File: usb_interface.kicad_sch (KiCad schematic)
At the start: 13 parts, among them J2 USB_B_Micro, U4 FT234XD-R

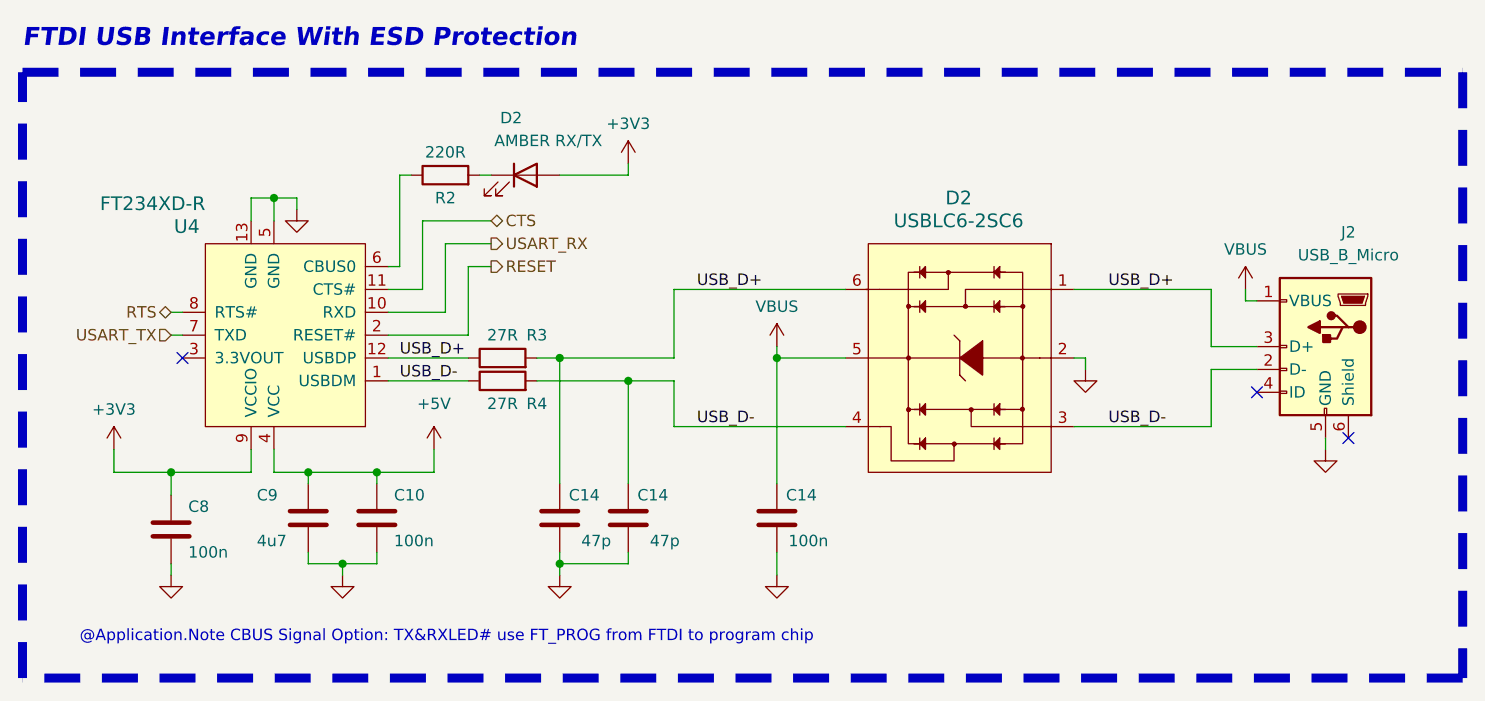
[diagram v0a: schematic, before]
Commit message: Added all schmatics about to change LDO 1 to buck
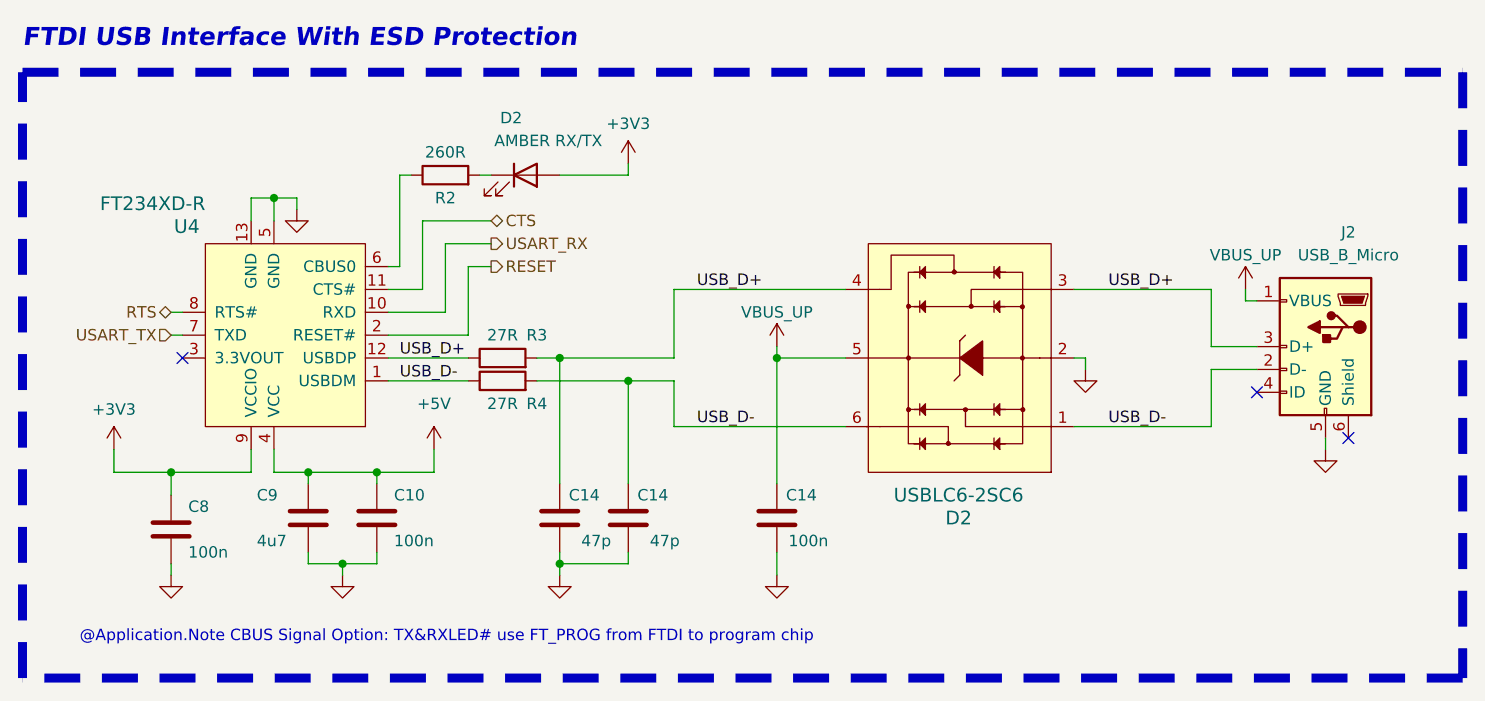
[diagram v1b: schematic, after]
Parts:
- C9: footprint Capacitor_SMD:C_0402_1005Metric -> Capacitor_SMD:C_0603_1608Metric
- J2: footprint Connector_USB:USB_Micro-B_Amphenol_10103594-0001LF_Horizontal -> Connector_USB:USB_Micro-B_Amphenol_10118194_Horizontal
- R2: value 220R -> 260R; footprint Resistor_SMD:R_0402_1005Metric -> Resistor_SMD:R_0603_1608Metric
- R3, R4: footprint Resistor_SMD:R_0402_1005Metric -> Resistor_SMD:R_0603_1608Metric
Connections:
- net USB_D+: now also D2.3, D2.4; no longer D2.1, D2.6
- net USB_D-: now also D2.1, D2.6; no longer D2.3, D2.4
- net VBUS renamed VBUS_UP
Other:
- moved on the sheet: D2
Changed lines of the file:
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@@
     (effects (font (size 1.27 1.27)) (justify left))
   )
-  (symbol (lib_id "dk_TVS-Diodes:USBLC6-2SC6") (at 127 86.36 0) (mirror y) (unit 1)
-    (in_bom yes) (on_board yes) (dnp no)
-    (property "Reference" "D2" (at 126.873 68.58 0)
+  (symbol (lib_id "dk_TVS-Diodes:USBLC6-2SC6") (at 127 86.36 180) (unit 1)
+    (in_bom yes) (on_board yes) (dnp no)
+    (property "Reference" "D2" (at 126.873 104.14 0)
       (effects (font (size 1.524 1.524)))
     )
-    (property "Value" "USBLC6-2SC6" (at 126.873 71.12 0)
+    (property "Value" "USBLC6-2SC6" (at 126.873 101.6 0)
       (effects (font (size 1.524 1.524)))
     )
-    (property "Footprint" "digikey-footprints:SOT23-6L" (at 121.92 81.28 0)
-      (effects (font (size 1.524 1.524)) (justify left) hide)
-    )
-    (property "Datasheet" "http://www.st.com/content/ccc/resource/technical/document/datasheet/06/1d/48/9c/6c/20/4a/b2/CD00050750.pdf/files/CD00050750.pdf/jcr:content/translations/en.CD00050750.pdf" (at 121.92 78.74 0)
-      (effects (font (size 1.524 1.524)) (justify left) hide)
-    )
-    (property "Digi-Key_PN" "497-5235-1-ND" (at 121.92 76.2 0)
-      (effects (font (size 1.524 1.524)) (justify left) hide)
-    )
-    (property "MPN" "USBLC6-2SC6" (at 121.92 73.66 0)
-      (effects (font (size 1.524 1.524)) (justify left) hide)
-    )
-    (property "Category" "Circuit Protection" (at 121.92 71.12 0)
-      (effects (font (size 1.524 1.524)) (justify left) hide)
-    )
-    (property "Family" "TVS - Diodes" (at 121.92 68.58 0)
-      (effects (font (size 1.524 1.524)) (justify left) hide)
-    )
-    (property "DK_Datasheet_Link" "http://www.st.com/content/ccc/resource/technical/document/datasheet/06/1d/48/9c/6c/20/4a/b2/CD00050750.pdf/files/CD00050750.pdf/jcr:content/translations/en.CD00050750.pdf" (at 121.92 66.04 0)
-      (effects (font (size 1.524 1.524)) (justify left) hide)
-    )
-    (property "DK_Detail_Page" "/product-detail/en/stmicroelectronics/USBLC6-2SC6/497-5235-1-ND/1121688" (at 121.92 63.5 0)
-      (effects (font (size 1.524 1.524)) (justify left) hide)
-    )
-    (property "Description" "TVS DIODE 5.25V 17V SOT23-6" (at 121.92 60.96 0)
-      (effects (font (size 1.524 1.524)) (justify left) hide)
-    )
-    (property "Manufacturer" "STMicroelectronics" (at 121.92 58.42 0)
-      (effects (font (size 1.524 1.524)) (justify left) hide)
-    )
-    (property "Status" "Active" (at 121.92 55.88 0)
+    (property "Footprint" "digikey-footprints:SOT23-6L" (at 121.92 91.44 0)
+      (effects (font (size 1.524 1.524)) (justify left) hide)
+    )
+    (property "Datasheet" "http://www.st.com/content/ccc/resource/technical/document/datasheet/06/1d/48/9c/6c/20/4a/b2/CD00050750.pdf/files/CD00050750.pdf/jcr:content/translations/en.CD00050750.pdf" (at 121.92 93.98 0)
+      (effects (font (size 1.524 1.524)) (justify left) hide)
+    )
+    (property "Digi-Key_PN" "497-5235-1-ND" (at 121.92 96.52 0)
+      (effects (font (size 1.524 1.524)) (justify left) hide)
+    )
+    (property "MPN" "USBLC6-2SC6" (at 121.92 99.06 0)
+      (effects (font (size 1.524 1.524)) (justify left) hide)
+    )
+    (property "Category" "Circuit Protection" (at 121.92 101.6 0)
+      (effects (font (size 1.524 1.524)) (justify left) hide)
+    )
+    (property "Family" "TVS - Diodes" (at 121.92 104.14 0)
+      (effects (font (size 1.524 1.524)) (justify left) hide)
+    )
+    (property "DK_Datasheet_Link" "http://www.st.com/content/ccc/resource/technical/document/datasheet/06/1d/48/9c/6c/20/4a/b2/CD00050750.pdf/files/CD00050750.pdf/jcr:content/translations/en.CD00050750.pdf" (at 121.92 106.68 0)
+      (effects (font (size 1.524 1.524)) (justify left) hide)
+    )
+    (property "DK_Detail_Page" "/product-detail/en/stmicroelectronics/USBLC6-2SC6/497-5235-1-ND/1121688" (at 121.92 109.22 0)
+      (effects (font (size 1.524 1.524)) (justify left) hide)
+    )
+    (property "Description" "TVS DIODE 5.25V 17V SOT23-6" (at 121.92 111.76 0)
+      (effects (font (size 1.524 1.524)) (justify left) hide)
+    )
+    (property "Manufacturer" "STMicroelectronics" (at 121.92 114.3 0)
+      (effects (font (size 1.524 1.524)) (justify left) hide)
+    )
+    (property "Status" "Active" (at 121.92 116.84 0)
       (effects (font (size 1.524 1.524)) (justify left) hide)
     )
@@
       (effects (font (size 1.27 1.27)))
     )
-    (property "Value" "220R" (at 69.85 63.5 90)
-      (effects (font (size 1.27 1.27)))
-    )
-    (property "Footprint" "Resistor_SMD:R_0402_1005Metric" (at 69.85 67.818 90)
+    (property "Value" "260R" (at 69.85 63.5 90)
+      (effects (font (size 1.27 1.27)))
+    )
+    (property "Footprint" "Resistor_SMD:R_0603_1608Metric" (at 69.85 67.818 90)
       (effects (font (size 1.27 1.27)) hide)
     )
@@
     )
   )
+  (symbol (lib_id "RF_Parts:VBUS_UP") (at 106.68 85.09 0) (unit 1)
+    (in_bom yes) (on_board yes) (dnp no)
+    (property "Reference" "#PWR0103" (at 106.68 88.9 0)
+      (effects (font (size 1.27 1.27)) hide)
+    )
+    (property "Value" "VBUS_UP" (at 106.68 81.28 0)
+      (effects (font (size 1.27 1.27)))
+    )
+    (property "Footprint" "" (at 106.68 85.09 0)
+      (effects (font (size 1.27 1.27)) hide)
+    )
+    (property "Datasheet" "" (at 106.68 85.09 0)
+      (effects (font (size 1.27 1.27)) hide)
+    )
+    (pin "1")
+    (instances
+      (project "CAN-USB RF Module"
+        (path "/05ffaa46-4df3-4c93-a015-882eb69d3f55/1b232830-45dc-4be3-ab16-3f2b1eb9ac0e"
+          (reference "#PWR0103") (unit 1)
+        )
+      )
+    )
+  )
   (symbol (lib_id "Device:C") (at 39.37 105.41 0) (unit 1)
     (in_bom yes) (on_board yes) (dnp no)
@@
       (effects (font (size 1.27 1.27)))
     )
-    (property "Footprint" "Resistor_SMD:R_0402_1005Metric" (at 76.2 88.138 90)
+    (property "Footprint" "Resistor_SMD:R_0603_1608Metric" (at 76.2 88.138 90)
       (effects (font (size 1.27 1.27)) hide)
     )
@@
       (effects (font (size 1.27 1.27)))
     )
-    (property "Footprint" "Connector_USB:USB_Micro-B_Amphenol_10103594-0001LF_Horizontal" (at 163.83 86.36 0)
+    (property "Footprint" "Connector_USB:USB_Micro-B_Amphenol_10118194_Horizontal" (at 163.83 86.36 0)
       (effects (font (size 1.27 1.27)) hide)
     )
@@
     )
   )
+  (symbol (lib_id "RF_Parts:VBUS_UP") (at 158.75 78.74 0) (unit 1)
+    (in_bom yes) (on_board yes) (dnp no)
+    (property "Reference" "#PWR0102" (at 158.75 82.55 0)
+      (effects (font (size 1.27 1.27)) hide)
+    )
+    (property "Value" "VBUS_UP" (at 158.75 74.93 0)
+      (effects (font (size 1.27 1.27)))
+    )
+    (property "Footprint" "" (at 158.75 78.74 0)
+      (effects (font (size 1.27 1.27)) hide)
+    )
+    (property "Datasheet" "" (at 158.75 78.74 0)
+      (effects (font (size 1.27 1.27)) hide)
+    )
+    (pin "1")
+    (instances
+      (project "CAN-USB RF Module"
+        (path "/05ffaa46-4df3-4c93-a015-882eb69d3f55/1b232830-45dc-4be3-ab16-3f2b1eb9ac0e"
+          (reference "#PWR0102") (unit 1)
+        )
+      )
+    )
+  )
   (symbol (lib_id "power:GND") (at 140.97 87.63 0) (unit 1)
     (in_bom yes) (on_board yes) (dnp no) (fields_autoplaced)
@@
       (effects (font (size 1.27 1.27)) (justify left))
     )
-    (property "Footprint" "Capacitor_SMD:C_0402_1005Metric" (at 55.5752 107.95 0)
+    (property "Footprint" "Capacitor_SMD:C_0603_1608Metric" (at 55.5752 107.95 0)
       (effects (font (size 1.27 1.27)) hide)
     )
@@
       (effects (font (size 1.27 1.27)))
     )
-    (property "Footprint" "Resistor_SMD:R_0402_1005Metric" (at 76.2 90.678 90)
+    (property "Footprint" "Resistor_SMD:R_0603_1608Metric" (at 76.2 90.678 90)
       (effects (font (size 1.27 1.27)) hide)
     )
@@
         )
       )
-    )
-  )
-  (symbol (lib_id "power:VBUS") (at 106.68 85.09 0) (unit 1)
-    (in_bom yes) (on_board yes) (dnp no) (fields_autoplaced)
-    (property "Reference" "#PWR023" (at 106.68 88.9 0)
-      (effects (font (size 1.27 1.27)) hide)
-    )
-    (property "Value" "VBUS" (at 106.68 80.645 0)
-      (effects (font (size 1.27 1.27)))
-    )
-    (property "Footprint" "" (at 106.68 85.09 0)
-      (effects (font (size 1.27 1.27)) hide)
-    )
-    (property "Datasheet" "" (at 106.68 85.09 0)
-      (effects (font (size 1.27 1.27)) hide)
-    )
-    (pin "1")
-    (instances
-      (project "CAN-USB RF Module"
-        (path "/05ffaa46-4df3-4c93-a015-882eb69d3f55"
-          (reference "#PWR023") (unit 1)
-        )
-        (path "/05ffaa46-4df3-4c93-a015-882eb69d3f55/1b232830-45dc-4be3-ab16-3f2b1eb9ac0e"
-          (reference "#PWR031") (unit 1)
-        )
-      )
-    )
-  )
-  (symbol (lib_id "power:VBUS") (at 158.75 78.74 0) (unit 1)
-    (in_bom yes) (on_board yes) (dnp no) (fields_autoplaced)
-    (property "Reference" "#PWR016" (at 158.75 82.55 0)
-      (effects (font (size 1.27 1.27)) hide)
-    )
-    (property "Value" "VBUS" (at 158.75 74.295 0)
-      (effects (font (size 1.27 1.27)))
-    )
-    (property "Footprint" "" (at 158.75 78.74 0)
-      (effects (font (size 1.27 1.27)) hide)
-    )
-    (property "Datasheet" "" (at 158.75 78.74 0)
-      (effects (font (size 1.27 1.27)) hide)
-    )
-    (pin "1")
-    (instances
-      (project "CAN-USB RF Module"
-        (path "/05ffaa46-4df3-4c93-a015-882eb69d3f55"
-          (reference "#PWR016") (unit 1)
-        )
-        (path "/05ffaa46-4df3-4c93-a015-882eb69d3f55/1b232830-45dc-4be3-ab16-3f2b1eb9ac0e"
-          (reference "#PWR034") (unit 1)
-        )
-      )

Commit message: Done design
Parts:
- J2: footprint Connector_USB:USB_Micro-B_Amphenol_10118194_Horizontal -> footprints:USB_Micro-B_Amphenol_10118194_Horizontal
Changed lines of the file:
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@@
       (effects (font (size 1.27 1.27)))
     )
-    (property "Footprint" "Connector_USB:USB_Micro-B_Amphenol_10118194_Horizontal" (at 163.83 86.36 0)
+    (property "Footprint" "footprints:USB_Micro-B_Amphenol_10118194_Horizontal" (at 163.83 86.36 0)
       (effects (font (size 1.27 1.27)) hide)
     )

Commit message: Added logo and assigned parts
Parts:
- C14: renamed from C8; JLC # (none) -> C327414
- C16: renamed from C10; JLC # (none) -> C327414
- C?: renamed from C14; JLC # (none) -> C327414
- D10: renamed from D2; value AMBER RX/TX -> AMBER; JLC # (none) -> C510024; JLC Link (none) -> https://jlcpcb.com/partdetail/RohmSemicon-SMLD12D8WT86/C510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; LCSC # (none) -> C2842814
- D?: renamed from D2; DK_Datasheet_Link http://www.st.com/content/ccc/resource/technical/document/d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 -> (none); DK_Detail_Page /product-detail/en/stmicroelectronics/USBLC6-2SC6/497-5235-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 -> (none); Digi-Key_PN 497-5235-1-ND -> (none); Family TVS - Diodes -> (none); LCSC # (none) -> C7519; MPN USBLC6-2SC6 -> (none); Manufacturer STMicroelectronics -> (none); Status Active -> (none)
- J4: renamed from J2; JLC # (none) -> C132562; LCSC # (none) -> C428495
- U5: renamed from U4; DK_Datasheet_Link http://www.ftdichip.com/Support/Documents/DataSheets/ICs/DS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 -> (none); DK_Detail_Page /product-detail/en/ftdi-future-technology-devices-internati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 -> (none); Digi-Key_PN 768-1178-1-ND -> (none); Family Interface - Controllers -> (none); LCSC # (none) -> C132158; MPN FT234XD-R -> (none); Manufacturer FTDI, Future Technology Devices International Ltd -> (none); Status Active -> (none)
- renumbered C9 to C15, C14 to C?, R2 to R17, R3 to R18, R4 to R19
